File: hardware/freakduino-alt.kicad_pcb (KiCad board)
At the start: 2 copper layers, 67 x 79.5 mm, 77 parts, among them J1 USB-MINI-AB, J2 POWERJACK/THRU-3, SW1 DIPSW4_DIP, U1 FT232-SSOP28, U2 TC1264, U3 AT86RF231, U4 GTL2003, U5 TPS61222, U6 ATMEGA328-QFP32, Y1 NX3225SA-16MHz-15ppm

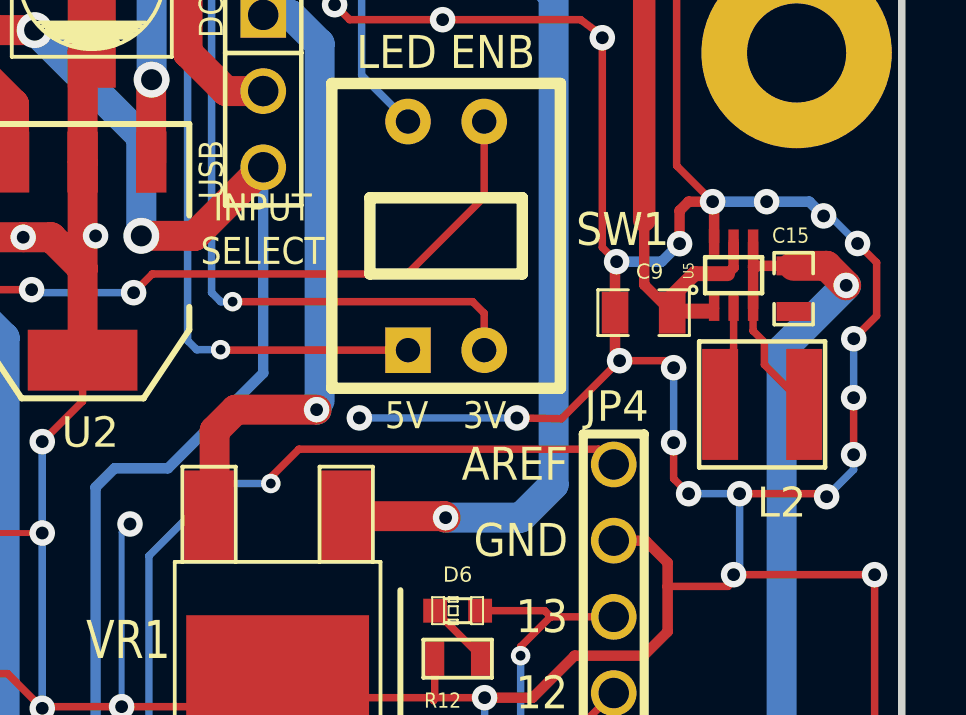
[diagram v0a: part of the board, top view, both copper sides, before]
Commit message: Attempting to update sch->brd netlist component footprint a for KiCAD v5+
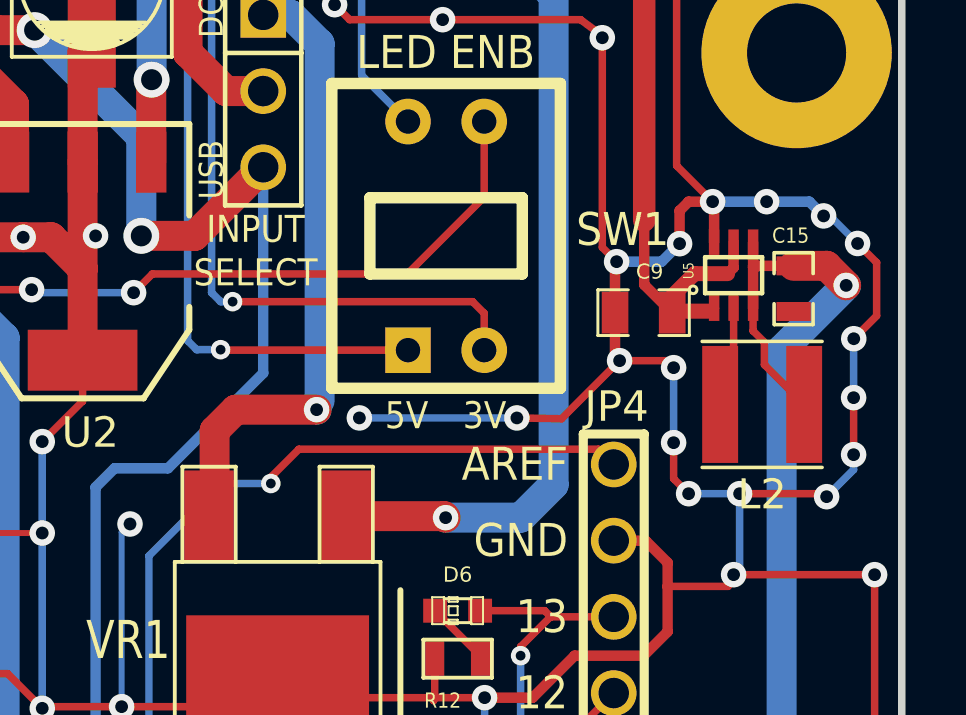
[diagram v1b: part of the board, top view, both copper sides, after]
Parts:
- L2: footprint NR1408 -> Inductor_SMD:L_Taiyo-Yuden_NR-40xx
- turned L2 to 180 degrees
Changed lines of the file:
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@@
   (layers
     (0 F.Cu signal)
-    (31 B.Cu signal)
-    (32 B.Adhes user)
-    (33 F.Adhes user)
-    (34 B.Paste user)
-    (35 F.Paste user)
-    (36 B.SilkS user)
+    (31 B.Cu signal hide)
+    (32 B.Adhes user hide)
+    (33 F.Adhes user hide)
+    (34 B.Paste user hide)
+    (35 F.Paste user hide)
+    (36 B.SilkS user hide)
     (37 F.SilkS user)
-    (38 B.Mask user)
-    (39 F.Mask user)
-    (40 Dwgs.User user)
-    (41 Cmts.User user)
-    (42 Eco1.User user)
-    (43 Eco2.User user)
+    (38 B.Mask user hide)
+    (39 F.Mask user hide)
+    (40 Dwgs.User user hide)
+    (41 Cmts.User user hide)
+    (42 Eco1.User user hide)
+    (43 Eco2.User user hide)
     (44 Edge.Cuts user)
   )
@@
     (add_net SLP_TR)
   )
+  (module Inductor_SMD:L_Taiyo-Yuden_NR-40xx (layer F.Cu)
+    (at 113.15 79.025 180)
+    (descr "Inductor, Taiyo Yuden, NR series, Taiyo-Yuden_NR-40xx, 4.0mmx4.0mm")
+    (tags "inductor taiyo-yuden nr smd")
+    (attr smd)
+    (fp_text reference L2 (at 0 -3 180) (layer F.SilkS)
+      (effects (font (size 1 1) (thickness 0.15)))
+    )
+    (fp_text value 4.7uH (at 0 3.5 180) (layer F.Fab)
+      (effects (font (size 1 1) (thickness 0.15)))
+    )
+    (fp_line (start 2.25 -2.25) (end -2.25 -2.25) (layer F.CrtYd) (width 0.05))
+    (fp_line (start 2.25 2.25) (end 2.25 -2.25) (layer F.CrtYd) (width 0.05))
+    (fp_line (start -2.25 2.25) (end 2.25 2.25) (layer F.CrtYd) (width 0.05))
+    (fp_line (start -2.25 -2.25) (end -2.25 2.25) (layer F.CrtYd) (width 0.05))
+    (fp_line (start -2 2.1) (end 2 2.1) (layer F.SilkS) (width 0.12))
+    (fp_line (start -2 -2.1) (end 2 -2.1) (layer F.SilkS) (width 0.12))
+    (fp_line (start -1.25 2) (end 0 2) (layer F.Fab) (width 0.1))
+    (fp_line (start -2 1.25) (end -1.25 2) (layer F.Fab) (width 0.1))
+    (fp_line (start -2 0) (end -2 1.25) (layer F.Fab) (width 0.1))
+    (fp_line (start 1.25 2) (end 0 2) (layer F.Fab) (width 0.1))
+    (fp_line (start 2 1.25) (end 1.25 2) (layer F.Fab) (width 0.1))
+    (fp_line (start 2 0) (end 2 1.25) (layer F.Fab) (width 0.1))
+    (fp_line (start 1.25 -2) (end 0 -2) (layer F.Fab) (width 0.1))
+    (fp_line (start 2 -1.25) (end 1.25 -2) (layer F.Fab) (width 0.1))
+    (fp_line (start 2 0) (end 2 -1.25) (layer F.Fab) (width 0.1))
+    (fp_line (start -1.25 -2) (end 0 -2) (layer F.Fab) (width 0.1))
+    (fp_line (start -2 -1.25) (end -1.25 -2) (layer F.Fab) (width 0.1))
+    (fp_line (start -2 0) (end -2 -1.25) (layer F.Fab) (width 0.1))
+    (fp_text user %R (at 0 0 180) (layer F.Fab)
+      (effects (font (size 1 1) (thickness 0.15)))
+    )
+    (pad 2 smd rect (at 1.4 0 180) (size 1.2 3.9) (layers F.Cu F.Paste F.Mask)
+      (net 30 N-0000032))
+    (pad 1 smd rect (at -1.4 0 180) (size 1.2 3.9) (layers F.Cu F.Paste F.Mask)
+      (net 64 VBAT))
+    (model ${KISYS3DMOD}/Inductor_SMD.3dshapes/L_Taiyo-Yuden_NR-40xx.wrl
+      (at (xyz 0 0 0))
+      (scale (xyz 1 1 1))
+      (rotate (xyz 0 0 0))
+    )
+  )
   (module SM0402_c (layer F.Cu)
     (at 62.5 75.25 90)
@@
     (pad 2 smd rect (at 0.9525 0 180) (size 0.889 1.397) (layers F.Cu F.Paste F.Mask)
       (net 35 N-0000053))
-    (model smd/chip_cms.wrl
+    (model ${KISYS3DMOD}/Inductor_SMD.3dshapes/L_0805_2012Metric.wrl
       (at (xyz 0 0 0))
-      (scale (xyz 0.1 0.1 0.1))
+      (scale (xyz 1 1 1))
       (rotate (xyz 0 0 0))
     )
@@
       (rotate (xyz 0 0 0))
     )
+    (model ${KISYS3DMOD}/Capacitor_SMD.3dshapes/C_0805_2012Metric.wrl
+      (at (xyz 0 0 0))
+      (scale (xyz 1 1 1))
+      (rotate (xyz 0 0 0))
+    )
   )
   (module SM0805 (layer F.Cu)
@@
     (pad 2 smd rect (at 0.9525 0 90) (size 0.889 1.397) (layers F.Cu F.Paste F.Mask)
       (net 69 VSS))
-    (model smd/chip_cms.wrl
+    (model ${KISYS3DMOD}/Capacitor_Tantalum_SMD.3dshapes/CP_EIA-2012-12_Kemet-R.wrl
       (at (xyz 0 0 0))
-      (scale (xyz 0.1 0.1 0.1))
+      (scale (xyz 1 1 1))
       (rotate (xyz 0 0 0))
     )
@@
       (rotate (xyz 0 0 0))
     )
+    (model ${KISYS3DMOD}/Capacitor_Tantalum_SMD.3dshapes/CP_EIA-2012-12_Kemet-R.wrl
+      (at (xyz 0 0 0))
+      (scale (xyz 1 1 1))
+      (rotate (xyz 0 0 0))
+    )
   )
   (module SM0603_Capa (layer F.Cu)
@@
     (pad 2 smd rect (at 0.762 0 270) (size 0.635 1.143) (layers F.Cu F.Paste F.Mask)
       (net 69 VSS))
-    (model smd\capacitors\C0603.wrl
-      (offset (xyz 0 0 0.001))
-      (scale (xyz 0.5 0.5 0.5))
+    (model ${KISYS3DMOD}/Capacitor_SMD.3dshapes/C_0603_1608Metric.wrl
+      (at (xyz 0 0 0))
+      (scale (xyz 1 1 1))
       (rotate (xyz 0 0 0))
     )
@@
     )
   )
-  (module NR1408 (layer F.Cu)
-    (at 113.15 79.025)
-    (fp_text reference L2 (at 0.65 3.275) (layer F.SilkS)
-      (effects (font (size 1 1) (thickness 0.2)))
-    )
-    (fp_text value 4.7uH (at 0.1 -0.9) (layer F.SilkS) hide
-      (effects (font (size 1 1) (thickness 0.15)))
-    )
-    (fp_line (start 2.1 -2.1) (end 2.1 2.1) (layer F.SilkS) (width 0.15))
-    (fp_line (start 2.1 2.1) (end -2.1 2.1) (layer F.SilkS) (width 0.15))
-    (fp_line (start -2.1 2.1) (end -2.1 -2.1) (layer F.SilkS) (width 0.15))
-    (fp_line (start -2.1 -2.1) (end 2.1 -2.1) (layer F.SilkS) (width 0.15))
-    (pad 1 smd rect (at 1.4 0) (size 1.2 3.7) (layers F.Cu F.Paste F.Mask)
-      (net 64 VBAT))
-    (pad 2 smd rect (at -1.4 0) (size 1.2 3.7) (layers F.Cu F.Paste F.Mask)
-      (net 30 N-0000032))
-    (model "$(KIPRJMOD)/share/modules/packages3d/inductor_NR1408.wrl"
-      (at (xyz 0 0 0))
-      (scale (xyz 1 1 1))
-      (rotate (xyz 0 0 0))
-    )
-  )
   (module crystal_C3E (layer F.Cu)
     (at 66.6496 85.1662 270)
@@
     (pad 2 smd rect (at 0.44958 0 90) (size 0.39878 0.59944) (layers F.Cu F.Paste F.Mask)
       (net 9 /RADIO/ANT))
-    (model smd\chip_cms.wrl
-      (offset (xyz 0 0 0.002))
-      (scale (xyz 0.05 0.05 0.05))
+    (model ${KISYS3DMOD}/Inductor_SMD.3dshapes/L_0402_1005Metric.wrl
+      (at (xyz 0 0 0))
+      (scale (xyz 1 1 1))
       (rotate (xyz 0 0 0))
     )
@@
     (effects (font (size 0.8 0.7) (thickness 0.13)))
   )
-  (gr_text "INPUT\nSELECT" (at 96.5 73.2) (layer F.SilkS)
+  (gr_text "INPUT\nSELECT" (at 96.266 73.914) (layer F.SilkS)
     (effects (font (size 0.9 0.8) (thickness 0.2)))
   )
@@
     (min_thickness 0.25)
     (keepout (tracks allowed) (vias allowed) (copperpour not_allowed))
-    (fill (arc_segments 16) (thermal_gap 0.5) (thermal_bridge_width 0.5) (smoothing fillet) (radius 1))
+    (fill (arc_segments 16) (thermal_gap 0.5) (thermal_bridge_width 0.5))
     (polygon
       (pts
@@
     (min_thickness 0.25)
     (keepout (tracks allowed) (vias allowed) (copperpour not_allowed))
-    (fill (arc_segments 16) (thermal_gap 0.5) (thermal_bridge_width 0.5) (smoothing fillet) (radius 1))
+    (fill (arc_segments 16) (thermal_gap 0.5) (thermal_bridge_width 0.5))
     (polygon
       (pts
@@
     (min_thickness 0.25)
     (keepout (tracks allowed) (vias allowed) (copperpour not_allowed))
-    (fill (arc_segments 16) (thermal_gap 0.5) (thermal_bridge_width 0.5) (smoothing fillet) (radius 1))
+    (fill (arc_segments 16) (thermal_gap 0.5) (thermal_bridge_width 0.5))
     (polygon
       (pts
@@
     (min_thickness 0.25)
     (keepout (tracks allowed) (vias allowed) (copperpour not_allowed))
-    (fill (arc_segments 16) (thermal_gap 0.5) (thermal_bridge_width 0.5) (smoothing fillet) (radius 1))
+    (fill (arc_segments 16) (thermal_gap 0.5) (thermal_bridge_width 0.5))
     (polygon
       (pts
@@
     (min_thickness 0.25)
     (keepout (tracks allowed) (vias allowed) (copperpour not_allowed))
-    (fill (arc_segments 16) (thermal_gap 0.5) (thermal_bridge_width 0.5) (smoothing fillet) (radius 1))
+    (fill (arc_segments 16) (thermal_gap 0.5) (thermal_bridge_width 0.5))
     (polygon
       (pts
@@
     (min_thickness 0.25)
     (keepout (tracks allowed) (vias allowed) (copperpour not_allowed))
-    (fill (arc_segments 16) (thermal_gap 0.5) (thermal_bridge_width 0.5) (smoothing fillet) (radius 1))
+    (fill (arc_segments 16) (thermal_gap 0.5) (thermal_bridge_width 0.5))
     (polygon
       (pts
